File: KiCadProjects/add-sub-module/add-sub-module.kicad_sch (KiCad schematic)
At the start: 24 parts, among them J1 2x4_Header, J2 1x2_Header, U1 CD74HCT10E, U2 SN74HCT00N, U3 SN74HCT02N, U4 SN74HCT257N, U5 CD74HCT04E

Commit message: final updates for Revision A
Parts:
- removed J1: 2x4_Header, Connector_PinHeader_2.54mm:PinHeader_2x04_P2.54mm_Vertical, symbol 0_add_sub:2x4_Header
- removed J2: 1x2_Header, Connector_PinHeader_2.54mm:PinHeader_1x02_P2.54mm_Vertical, symbol 0_add_sub:1x2_Header
- added H1, H2, H3, H4: MountingHole_Pad, MountingHole:MountingHole_3.2mm_M3_DIN965_Pad, symbol Mechanical:MountingHole_Pad
- added J1, J2: Conn_01x04_Pin, Connector_PinHeader_2.54mm:PinHeader_1x04_P2.54mm_Vertical, symbol Connector:Conn_01x04_Pin
- added J3: Conn_01x02_Pin, Connector_PinHeader_2.54mm:PinHeader_1x02_P2.54mm_Vertical, symbol Connector:Conn_01x02_Pin
- C1, C2, C3, C4, C5: footprint Capacitor_THT:C_Disc_D4.7mm_W2.5mm_P5.00mm -> Capacitor_THT:C_Disc_D5.0mm_W2.5mm_P5.00mm; LCSC (none) -> C2761729; Link https://www.newark.com/multicomp/mc0805b104k500a5-08mm/cera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 -> https://www.lcsc.com/product-detail/Through-Hole-Ceramic-Ca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; Part No (none) -> C2761729
- D1, D2, D3, D4: LCSC (none) -> C779442; Link (none) -> https://www.lcsc.com/product-detail/LED-Indication-Discrete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; Part No (none) -> C779442
- D5, D6: LCSC (none) -> C779439; Link (none) -> https://www.lcsc.com/product-detail/LED-Indication-Discrete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; Part No (none) -> C779439
- R1, R2, R3, R4, R5, R6: value 1k -> 330; LCSC (none) -> C2935230; Link (none) -> https://www.lcsc.com/product-detail/Through-Hole-Resistors_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; Part No (none) -> C2935230
- U1: LCSC CD74HCT10E -> C2325; Link https://www.digikey.com/en/products/detail/texas-instrument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 -> https://www.lcsc.com/product-detail/IC-Transistor-Socket_BO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
- U2: LCSC SN74HCT00N -> C2325; Link https://www.digikey.com/en/products/detail/texas-instrument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 -> https://www.lcsc.com/product-detail/IC-Transistor-Socket_BO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
- U3: LCSC SN74HCT02N -> C2325; Link https://www.digikey.com/en/products/detail/texas-instrument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 -> https://www.lcsc.com/product-detail/IC-Transistor-Socket_BO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
- U4: LCSC SN74HCT257N -> C2326; Link https://www.digikey.com/en/products/detail/texas-instrument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 -> https://www.lcsc.com/product-detail/IC-Transistor-Socket_BO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
- U5: LCSC CD74HCT04E -> C2325; Link https://www.digikey.com/en/products/detail/texas-instrument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 -> https://www.lcsc.com/product-detail/IC-Transistor-Socket_BO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
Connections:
- net +5V: now also J1.1 (Pin_1)
- net ADD/SUB: now also J2.4 (Pin_4)
- net CA: now also J2.2 (Pin_2)
- net CARRY: now also J2.3 (Pin_3)
- net CLK: now also J1.2 (Pin_2)
- net COUT: now also J3.2 (Pin_2)
- net GND: now also H1.1, H2.1, H3.1, H4.1, J1.4 (Pin_4)
- net KA: now also J2.1 (Pin_1)
- net RST: now also J1.3 (Pin_3)
- net SUM: now also J3.1 (Pin_1)
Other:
- moved on the sheet: D1, D2, D3, D4, D5, D6, R1, R2, R3, R4, R5, R6

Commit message: FINAL final changes for Rev. A
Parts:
- U1: value CD74HCT10E -> IC-14P
- U2: value SN74HCT00N -> IC-14P
- U3: value SN74HCT02N -> IC-14P
- U4: value SN74HCT257N -> IC-16P
- U5: value CD74HCT04E -> IC-14P
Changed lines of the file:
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@@
 			)
 		)
-		(property "Value" "CD74HCT04E"
+		(property "Value" "IC-14P"
 			(at 232.156 80.518 90)
 			(effects
@@
 			)
 		)
-		(property "Datasheet" "CD74HCT04E"
+		(property "Datasheet" ""
 			(at 231.14 114.3 0)
 			(effects
@@
 			)
 		)
-		(property "Description" ""
+		(property "Description" "CD74HCT04E"
 			(at 231.14 114.3 0)
 			(effects
@@
 			)
 		)
-		(property "Value" "CD74HCT10E"
+		(property "Value" "IC-14P"
 			(at 41.656 80.264 90)
 			(effects
@@
 			)
 		)
-		(property "Datasheet" "CD74HCT10E"
+		(property "Datasheet" ""
 			(at 40.64 114.3 0)
 			(effects
@@
 			)
 		)
-		(property "Description" ""
+		(property "Description" "CD74HCT10E"
 			(at 40.64 114.3 0)
 			(effects
@@
 			)
 		)
-		(property "Value" "SN74HCT02N"
+		(property "Value" "IC-14P"
 			(at 135.128 80.264 90)
 			(effects
@@
 			)
 		)
-		(property "Datasheet" "SN74HCT02N"
+		(property "Datasheet" ""
 			(at 134.62 114.3 0)
 			(effects
@@
 			)
 		)
-		(property "Description" ""
+		(property "Description" "SN74HCT02N"
 			(at 134.62 114.3 0)
 			(effects
@@
 			)
 		)
-		(property "Value" "SN74HCT00N"
+		(property "Value" "IC-14P"
 			(at 87.376 80.264 90)
 			(effects
@@
 			)
 		)
-		(property "Datasheet" "SN74HCT00N"
+		(property "Datasheet" ""
 			(at 86.36 114.3 0)
 			(effects
@@
 			)
 		)
-		(property "Description" ""
+		(property "Description" "SN74HCT00N"
 			(at 86.36 114.3 0)
 			(effects
@@
 			)
 		)
-		(property "Value" "SN74HCT257N"
+		(property "Value" "IC-16P"
 			(at 181.356 80.01 90)
 			(effects
@@
 			)
 		)
-		(property "Datasheet" "SN74HCT257N"
+		(property "Datasheet" ""
 			(at 180.34 114.3 0)
 			(effects
@@
 			)
 		)
-		(property "Description" ""
+		(property "Description" "SN74HCT257N"
 			(at 180.34 114.3 0)
 			(effects

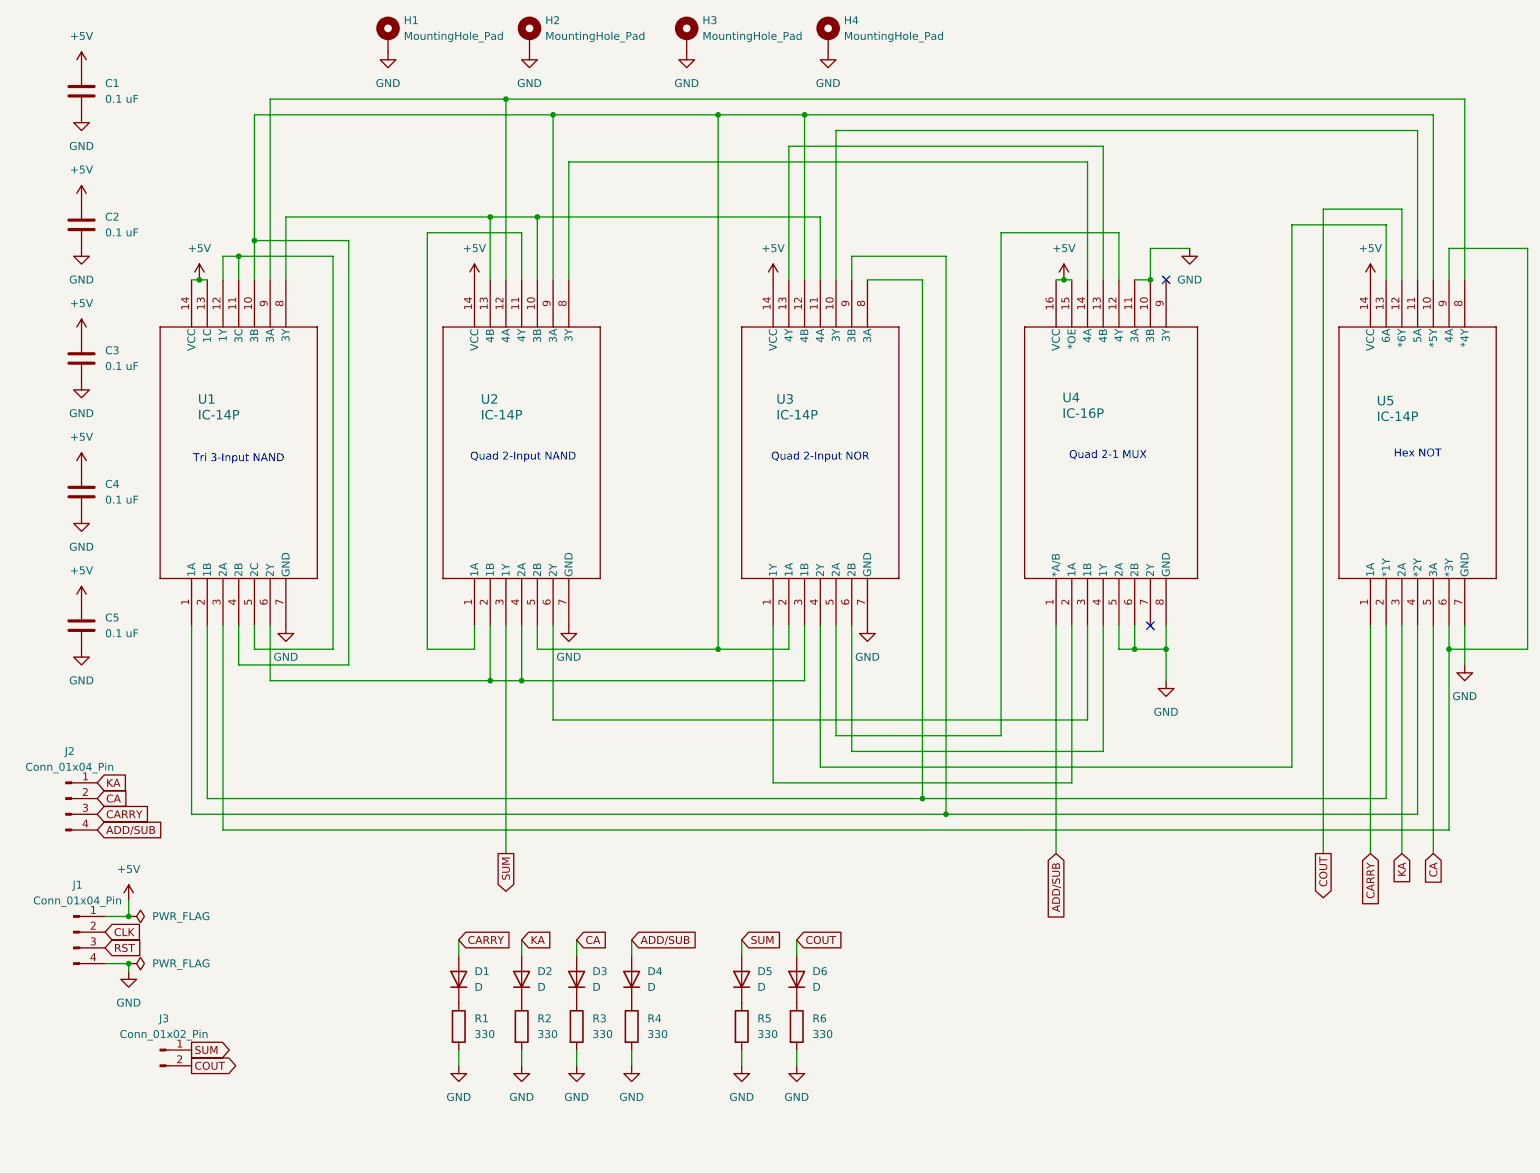
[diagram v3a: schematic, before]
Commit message: Small changes to PCB, grounded MUX OE pin and updated PCB from schematic
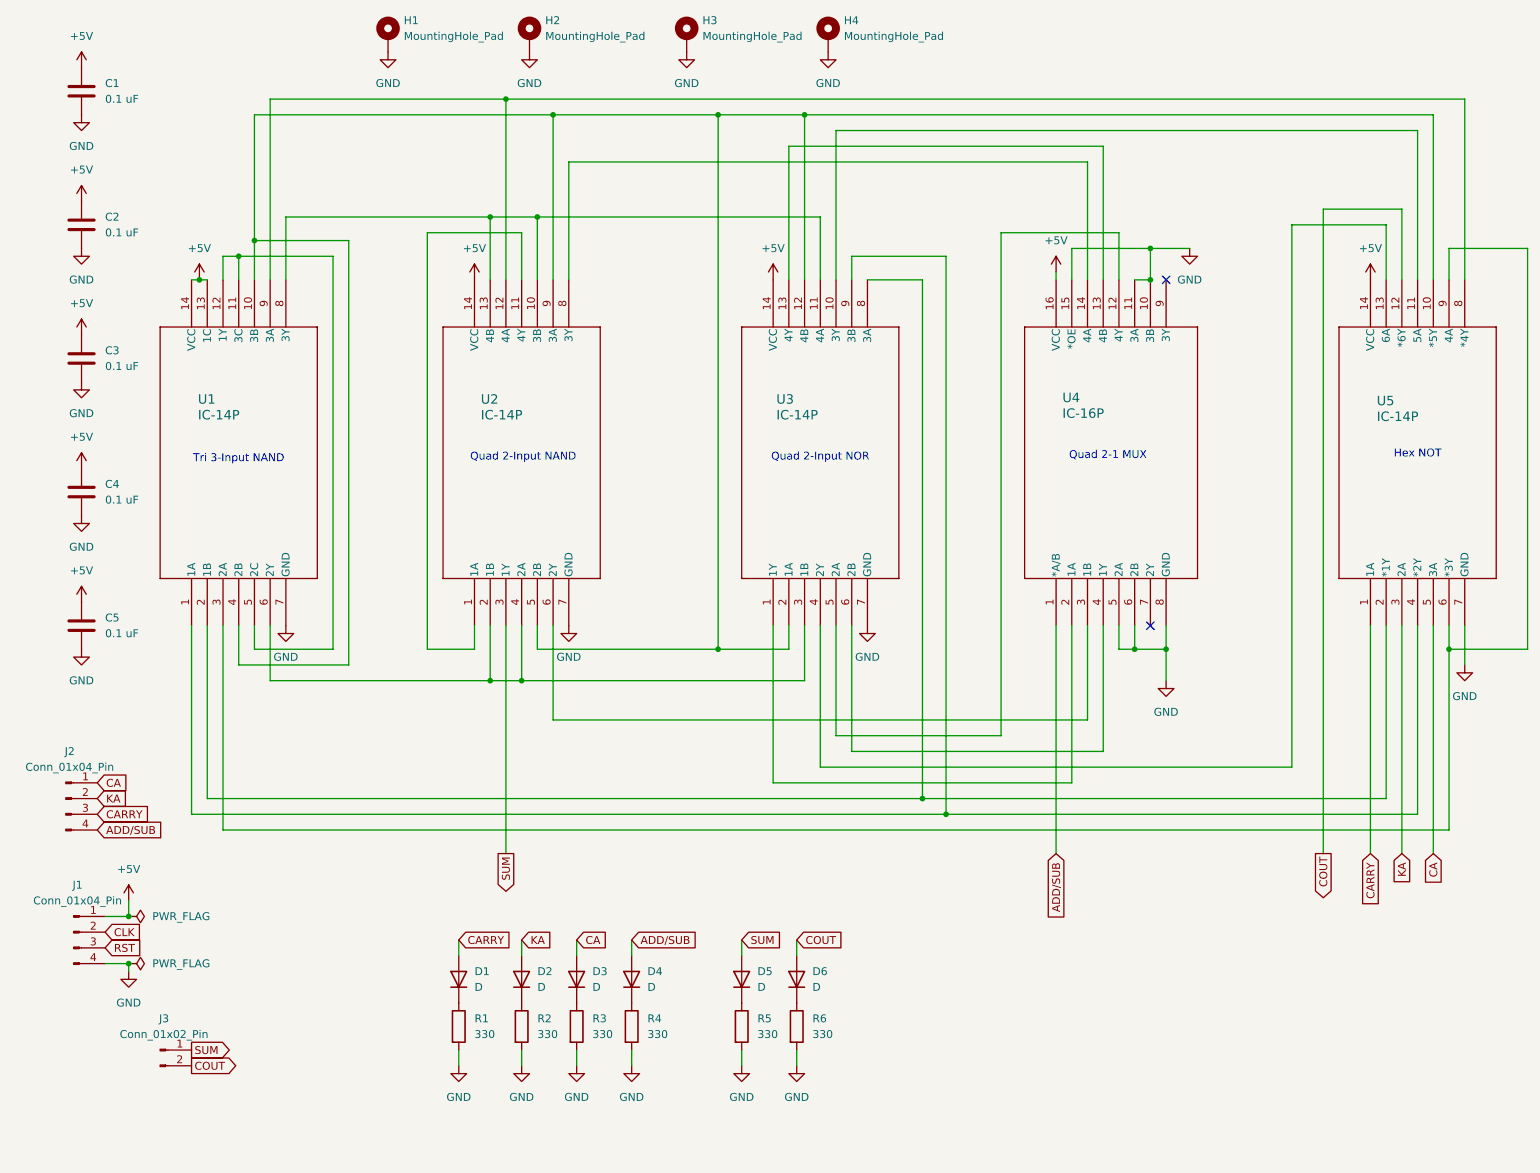
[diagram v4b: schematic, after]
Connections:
- net +5V: no longer U4.15 (*OE)
- net CA: now also J2.1 (Pin_1); no longer J2.2 (Pin_2)
- net GND: now also U4.15 (*OE)
- net KA: now also J2.2 (Pin_2); no longer J2.1 (Pin_1)
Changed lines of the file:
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@@
 	)
 	(junction
-		(at 181.61 58.42)
-		(diameter 0)
-		(color 0 0 0 0)
-	)
-	(junction
 		(at 96.52 48.26)
 		(diameter 0)
@@
 	)
 	(junction
+		(at 195.58 53.34)
+		(diameter 0)
+		(color 0 0 0 0)
+	)
+	(junction
 		(at 88.9 48.26)
 		(diameter 0)
@@
 	(wire
 		(pts
+			(xy 180.34 57.15) (xy 180.34 58.42)
+		)
+		(stroke
+			(width 0)
+			(type default)
+		)
+	)
+	(wire
+		(pts
 			(xy 125.73 31.75) (xy 99.06 31.75)
 		)
@@
 	(wire
 		(pts
+			(xy 182.88 53.34) (xy 195.58 53.34)
+		)
+		(stroke
+			(width 0)
+			(type default)
+		)
+	)
+	(wire
+		(pts
 			(xy 236.22 58.42) (xy 236.22 46.99)
 		)
@@
 	(wire
 		(pts
+			(xy 182.88 58.42) (xy 182.88 53.34)
+		)
+		(stroke
+			(width 0)
+			(type default)
+		)
+	)
+	(wire
+		(pts
 			(xy 48.26 54.61) (xy 63.5 54.61)
 		)
@@
 	(wire
 		(pts
-			(xy 181.61 58.42) (xy 182.88 58.42)
-		)
-		(stroke
-			(width 0)
-			(type default)
-		)
-	)
-	(wire
-		(pts
 			(xy 101.6 39.37) (xy 185.42 39.37)
 		)
@@
 	(wire
 		(pts
-			(xy 180.34 58.42) (xy 181.61 58.42)
-		)
-		(stroke
-			(width 0)
-			(type default)
-		)
-	)
-	(wire
-		(pts
 			(xy 99.06 31.75) (xy 99.06 58.42)
 		)
@@
 		)
 	)
-	(global_label "KA"
+	(global_label "CA"
 		(shape input)
 		(at 25.4 139.7 0)
@@
 		)
 	)
-	(global_label "CA"
+	(global_label "KA"
 		(shape input)
 		(at 25.4 142.24 0)
@@
 	(symbol
 		(lib_id "power:+5V")
-		(at 181.61 58.42 0)
+		(at 180.34 57.15 0)
 		(unit 1)
 		(exclude_from_sim no)
@@
 		(fields_autoplaced yes)
 		(property "Reference" "#PWR010"
-			(at 181.61 62.23 0)
+			(at 180.34 60.96 0)
 			(effects
 				(font
@@
 		)
 		(property "Value" "+5V"
-			(at 181.61 53.34 0)
+			(at 180.34 52.07 0)
 			(effects
 				(font
@@
 		)
 		(property "Footprint" ""
-			(at 181.61 58.42 0)
+			(at 180.34 57.15 0)
 			(effects
 				(font
@@
 		)
 		(property "Datasheet" ""
-			(at 181.61 58.42 0)
+			(at 180.34 57.15 0)
 			(effects
 				(font
@@
 		)
 		(property "Description" "Power symbol creates a global label with name \"+5V\""
-			(at 181.61 58.42 0)
+			(at 180.34 57.15 0)
 			(effects
 				(font
